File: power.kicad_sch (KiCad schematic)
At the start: 80 parts, among them CON2 BARREL_JACK, P5 CONN_01X01, P7 CONN_01X01, P8 CONN_01X01, U17 LMR51420, U18 LMR51420, U19 LMR51420, U20 LP5907-3.0, U21 LP2985A-10DBVR, U22 LD3920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

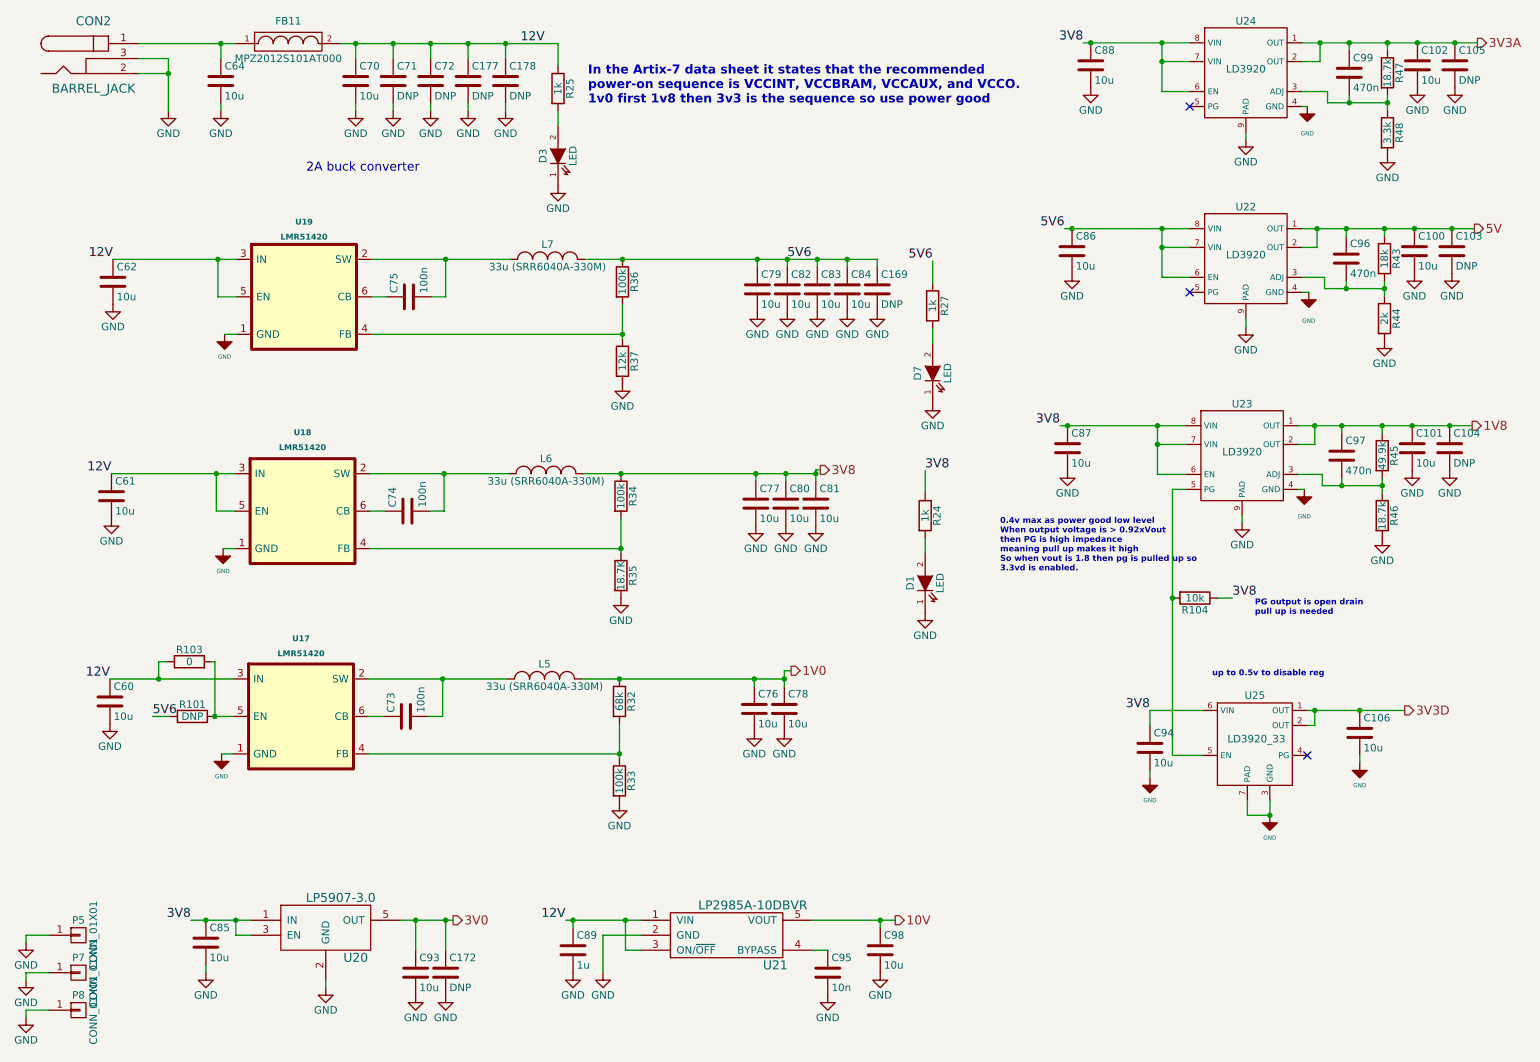
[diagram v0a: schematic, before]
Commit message: DNP components are deleted
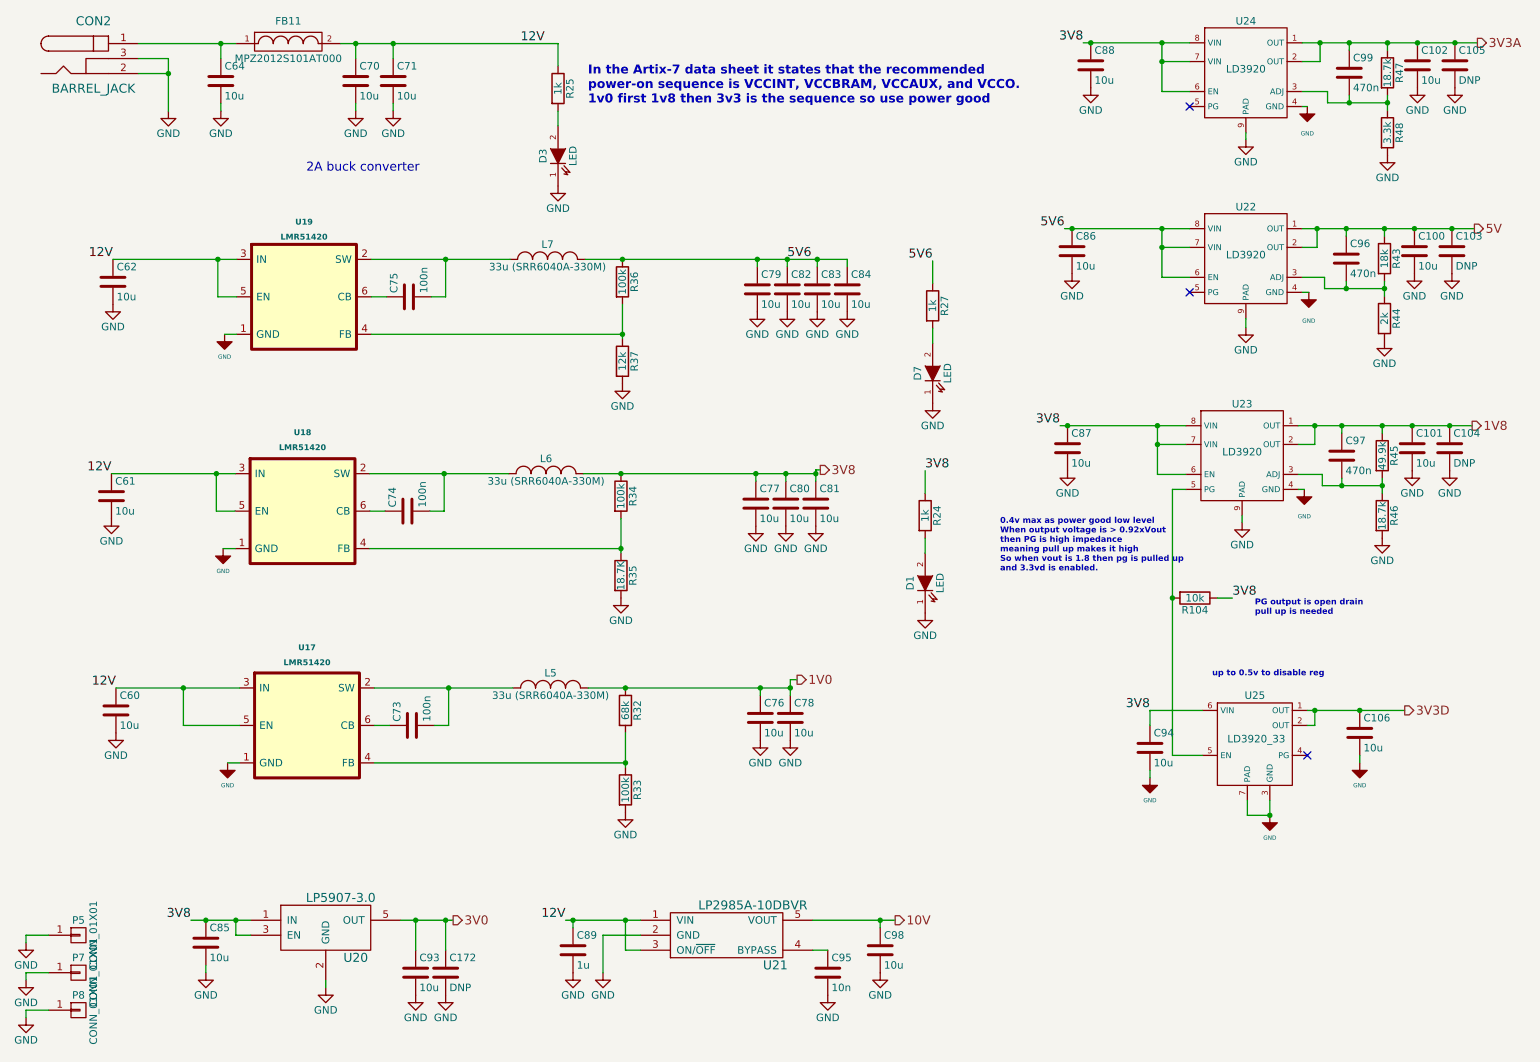
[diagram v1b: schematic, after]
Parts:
- removed C169, C177, C178, C72: DNP, Footprints:SMD_0805, symbol fmcw3-rescue:C
- removed R101: DNP, Footprints:SMD_0402, symbol fmcw3-rescue:R
- removed R103: 0, Footprints:SMD_0402, symbol fmcw3-rescue:R
- C71: value DNP -> 10u
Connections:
- net 12V: now also U17.5 (EN)
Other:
- note added: "0.4v max as power good low level When output voltage is > 0.92xVout then PG is high impedance meaning pull up makes it high So when vout is 1.8 then pg is pulled up and 3.3vd is enabled."
- note removed: "0.4v max as power good low level When output voltage is > 0.92xVout then PG is high impedance meaning pull up makes it high So when vout is 1.8 then pg is pulled up so 3.3vd is enabled."
- moved on the sheet: C60, C73, C76, C78, L5, R32, R33, U17

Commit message: pcb is checked dnp is deleted copper pours are checked
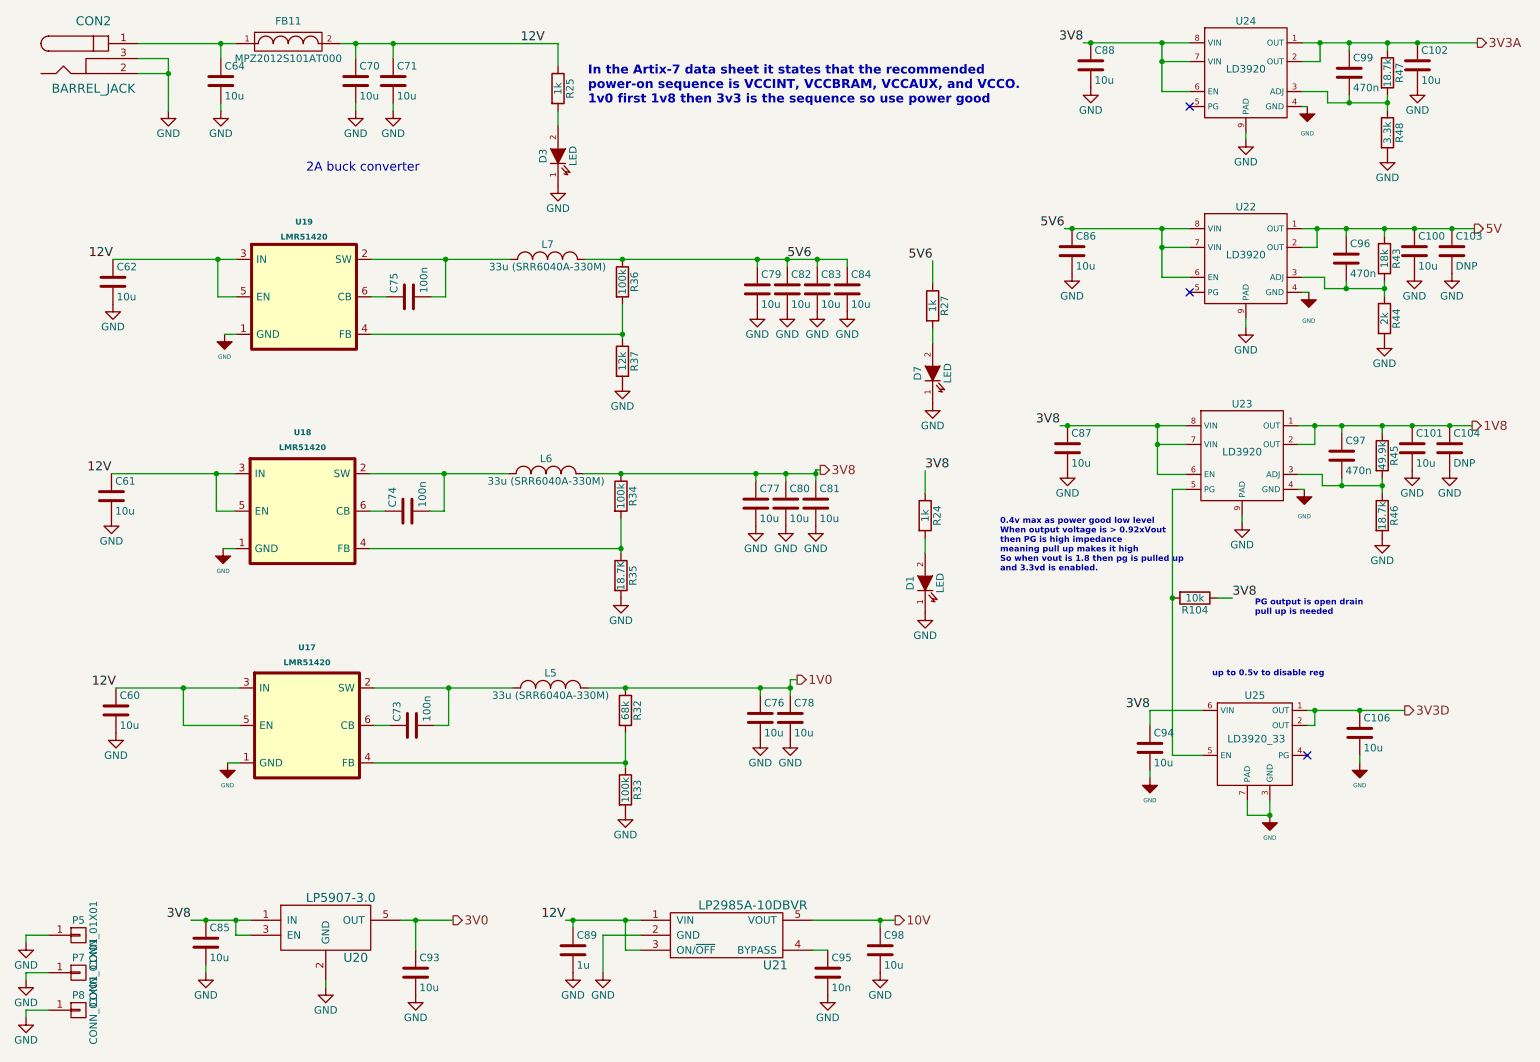
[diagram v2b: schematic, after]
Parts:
- removed C105, C172: DNP, Footprints:SMD_0805, symbol fmcw3-rescue:C
